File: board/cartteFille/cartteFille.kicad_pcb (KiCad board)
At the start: 2 copper layers, 65 parts, among them U11 MAX4040EUKT, U20 MCP23018-E/SS, U21-2 SN74LVC2G14DBVTG4, U23-4 SN74LVC2G14DBVTG4, U25-6 SN74LVC2G14DBVTG4, U27-8 SN74LVC2G14DBVTG4

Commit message: push sous schémat
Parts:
- moved S27 124.7 mm to (127.5, 147.6)
- moved D25 120.6 mm to (137.9, 96.8)
- moved R253 120.6 mm to (138.0, 96.8)
- moved S25 119.9 mm to (127.8, 94.5)
- moved S28 114.7 mm to (126.7, 120.1)
- moved D26 114.3 mm to (137.7, 68.1)
- moved R263 114.3 mm to (137.7, 68.1)
- moved S26 113.8 mm to (128.0, 65.5)
- moved R261 109.7 mm to (115.6, 68.1)
- moved C261 109.7 mm to (115.6, 73.2)
- moved R251 109.2 mm to (118.1, 82.5)
- moved C251 109.2 mm to (118.1, 87.6)
- moved U25-6 108.8 mm to (107.4, 81.0)
- moved R271 108.2 mm to (119.1, 135.6)
- moved R252 105.9 mm to (128.0, 81.9), turned to 90 degrees
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
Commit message: resistor tab adding
on rajoute une table de résistance pour le changement facile de boutons
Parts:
- moved U21-2 3.75 mm to (44.5, 78.0)

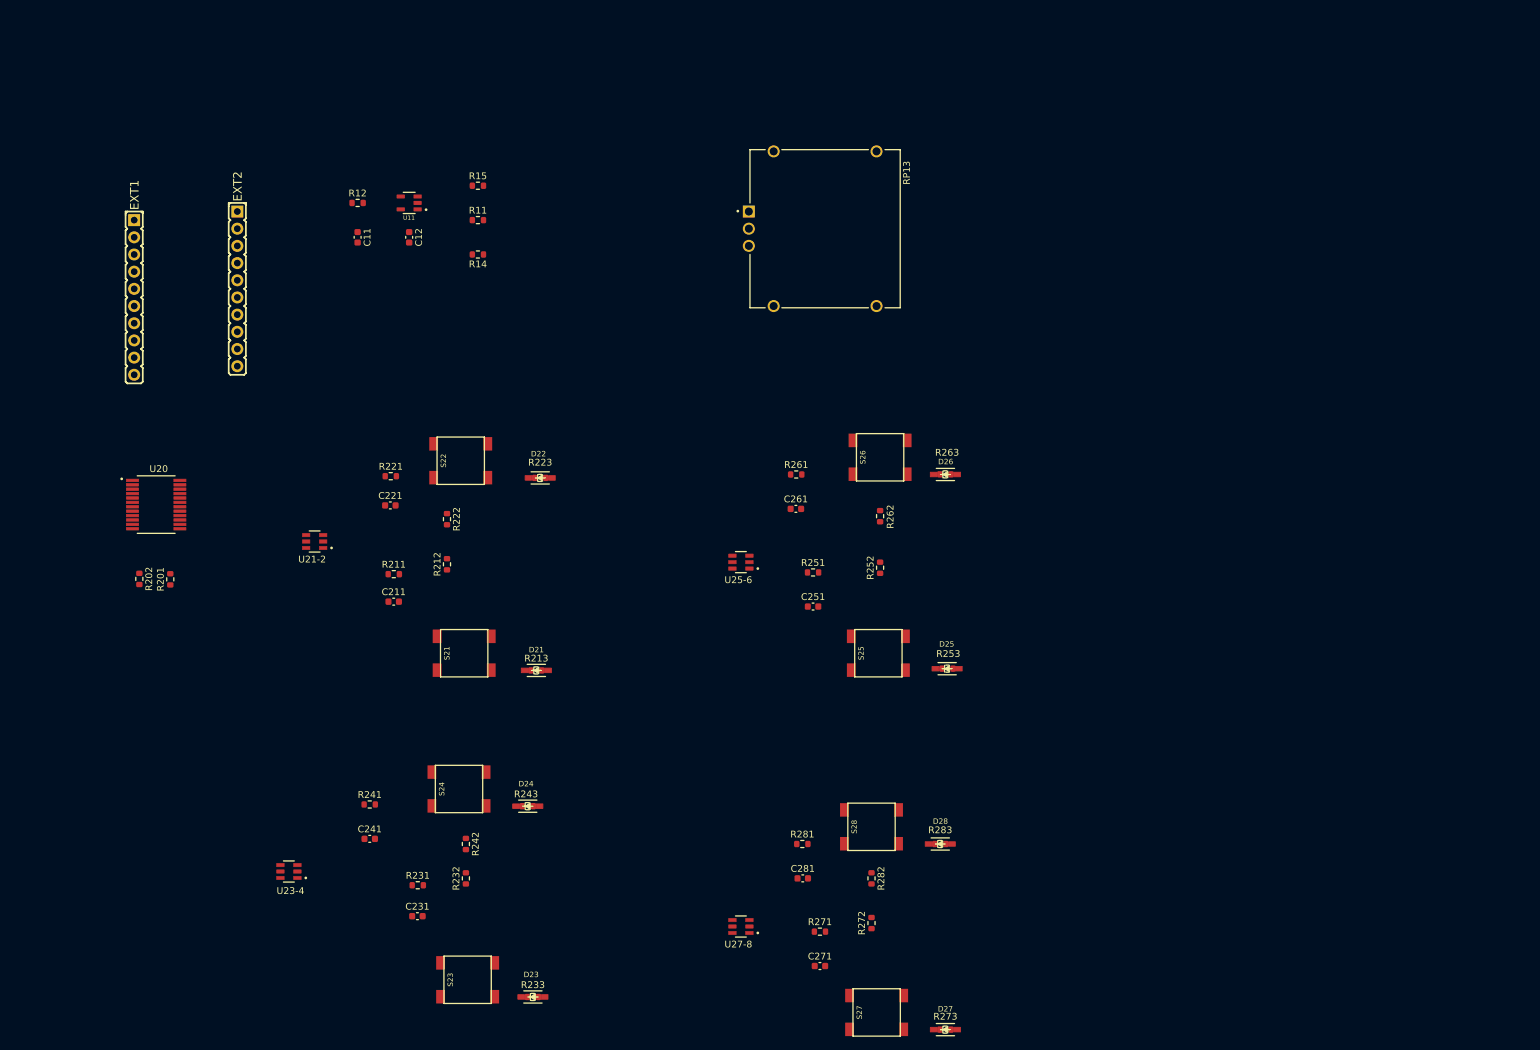
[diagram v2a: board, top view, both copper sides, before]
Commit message: commit début placage
début du placage sans les bouttons
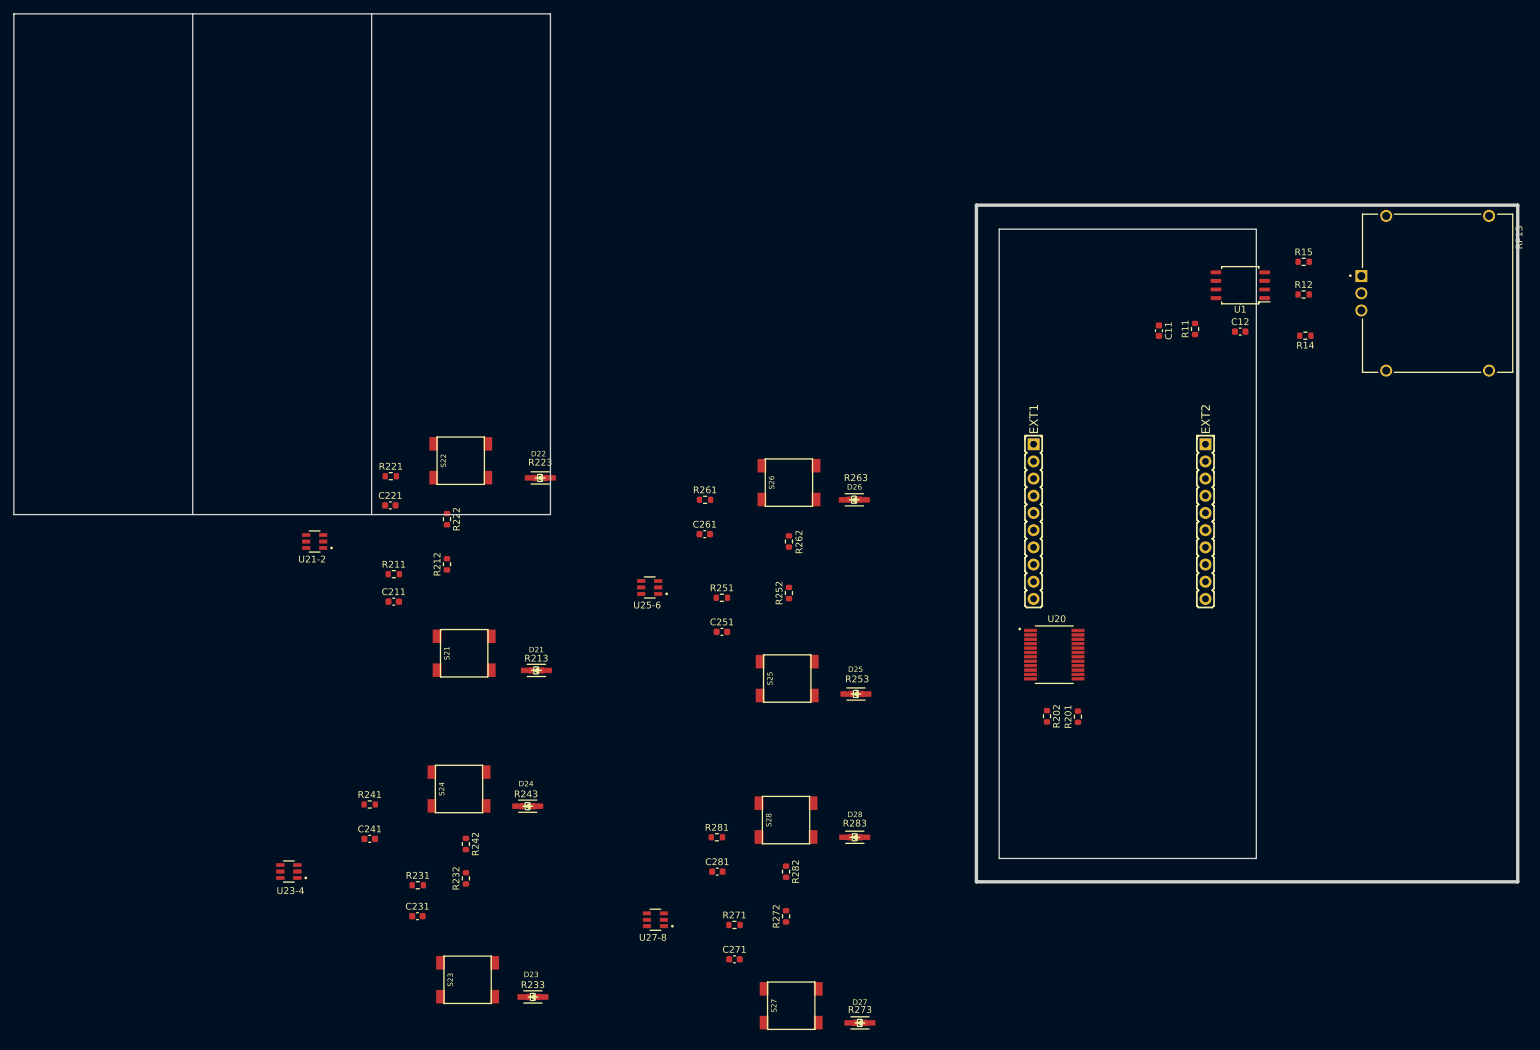
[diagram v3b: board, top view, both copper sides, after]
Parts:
- removed U11: MAX4040EUKT, MAX4040EUKT:SOT95P280X145-5N
- added U1: LM358, Package_SO:SOIC-8_5.275x5.275mm_P1.27mm, F.Cu at (181.2, 40.1)
- R11: value 150Ohm -> 10KOhm
- R12: value 10KOhm -> 150Ohm
- moved EXT2 147.2 mm to (176.1, 75.0)
- moved R12 140.5 mm to (190.6, 41.5)
- moved EXT1 137.0 mm to (150.7, 75.0)
- moved R201 135.7 mm to (157.3, 103.9)
- moved R202 135.7 mm to (152.7, 103.8)
- moved U20 134.6 mm to (153.8, 94.7)
- moved C12 123.6 mm to (181.2, 47.0), turned to 0 degrees
- moved R14 122.9 mm to (190.9, 47.6)
- moved R15 122.5 mm to (190.6, 36.6)
- moved C11 119.2 mm to (169.2, 46.8)
- moved R11 107.2 mm to (174.6, 46.6), turned to 90 degrees
- moved RP13 91.0 mm to (210.4, 41.3)
- moved R253 14.0 mm to (124.5, 100.5)
- moved D26 14.0 mm to (124.2, 71.8)
- moved R261 14.0 mm to (102.1, 71.8)
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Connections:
- EXT1 pad 8: /GPIO3-U20RESET -> unconnected-(EXT1-Pad8)
- EXT2 pad 2: /ADC_CH0-U11RP1 -> unconnected-(EXT2-Pad2)
- EXT2 pad 3: unconnected-(EXT2-Pad3) -> /ADC_CH0-U11RP1
- EXT2 pad 5: /GPIO33-INTA -> unconnected-(EXT2-Pad5)
- R11 pad 1: Net-(R11-Pad1) -> GND
- R11 pad 2: Net-(R11-Pad2) -> /ADC_CH0-U11RP1
- R12 pad 1: /ADC_CH0-U11RP1 -> Net-(R12-Pad1)
- RP13 pad 2: Net-(R11-Pad2) -> Net-(R12-Pad1)
- U20 pad 16: /GPIO33-INTA -> unconnected-(U20-Pad16)
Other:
- board outline added: 222.2 x 128.3 mm

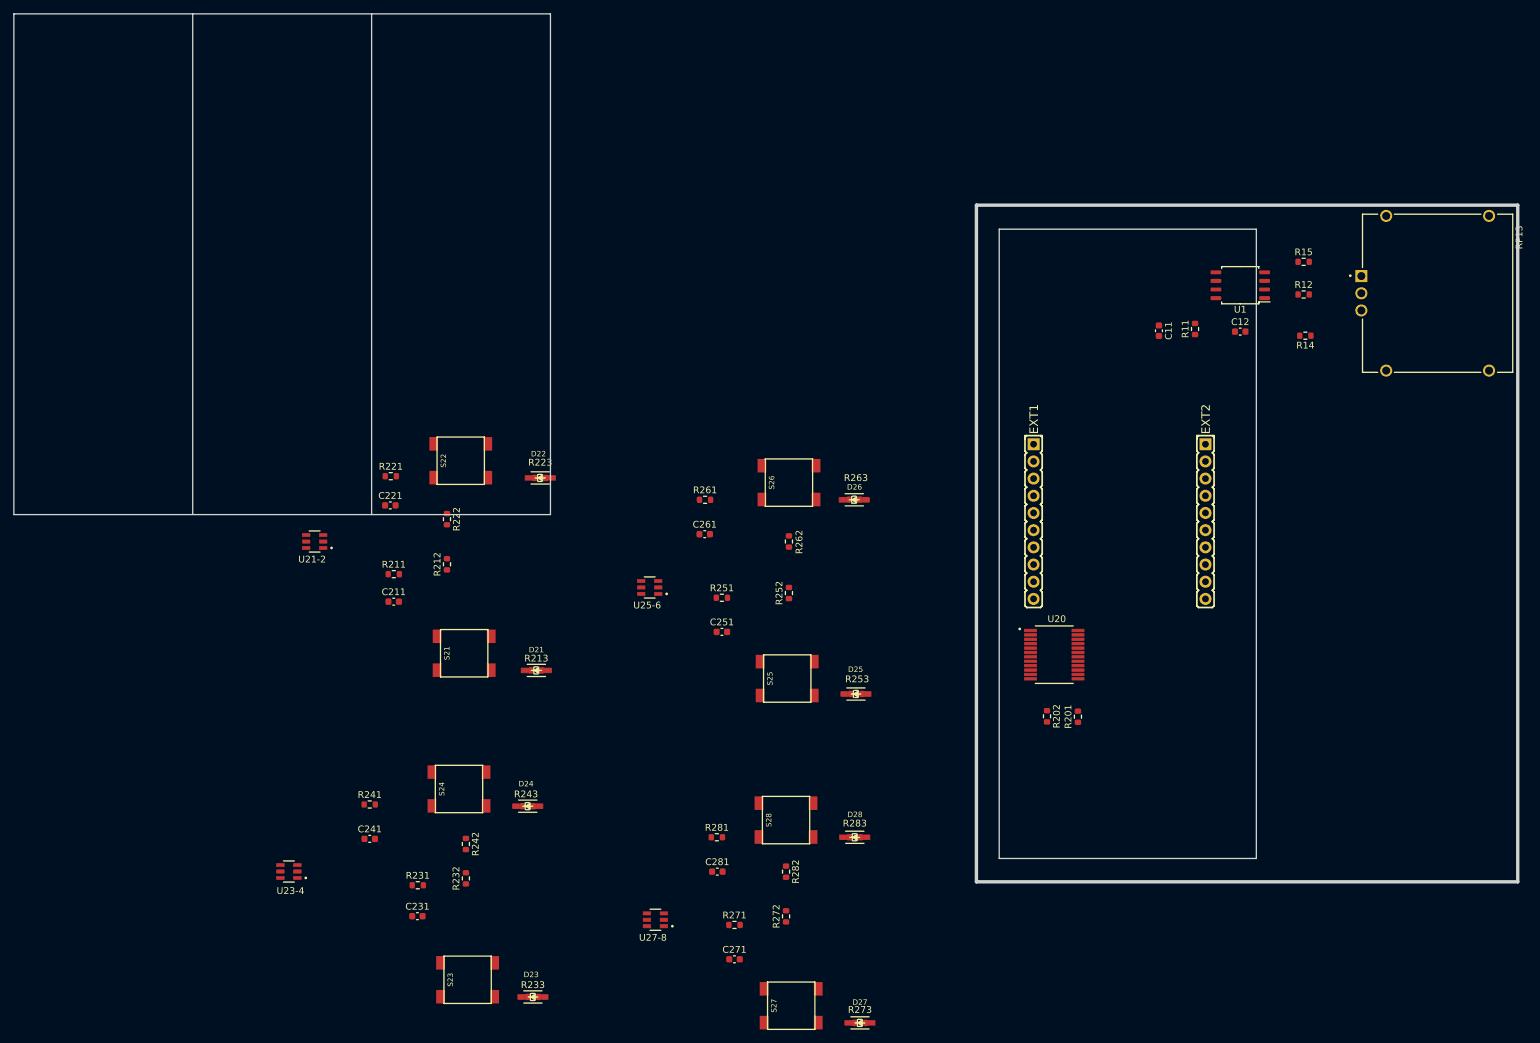
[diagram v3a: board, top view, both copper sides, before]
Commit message: placage de bouton approximatif
tous les composant ont été placé approximativement à des places qui simplifie les connexion entre ceux-ci. Il faudra encore adapter le disign en fonction des dimensions exactes du pcb et des volonté de placement de l'entreprise. puis créer une version clean. pour le moment pcb de 80x100 et placage des bouton en 2 colonnes de 4 botons avec une parie réservée au potentiomètre
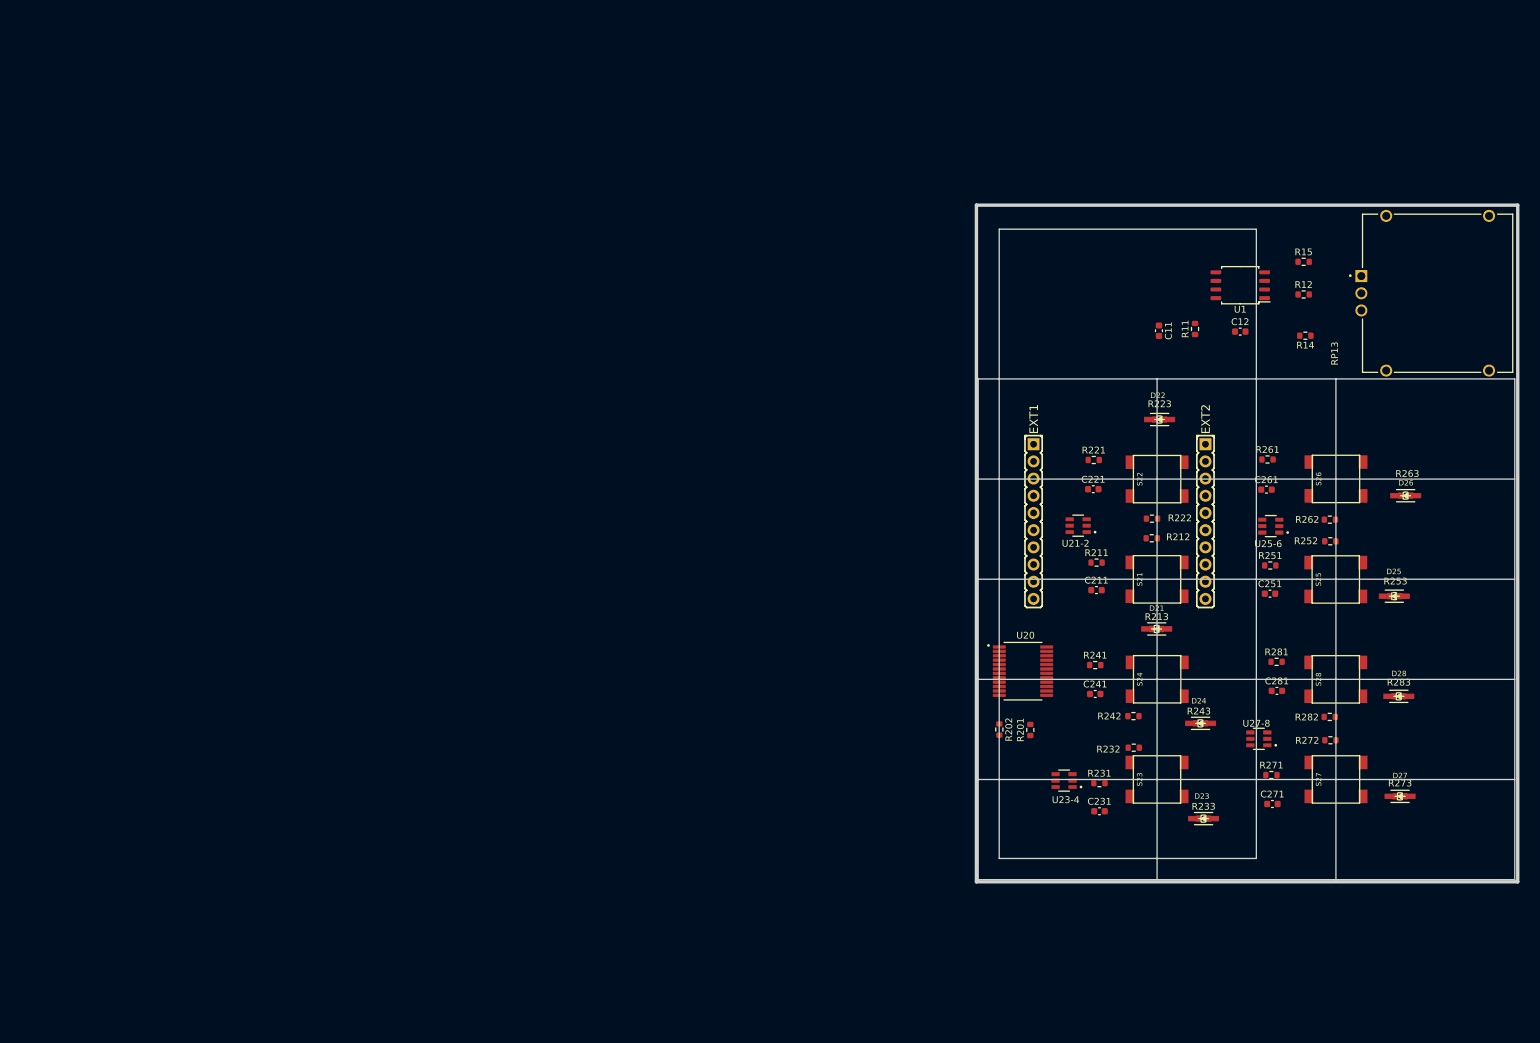
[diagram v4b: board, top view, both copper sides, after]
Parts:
- moved U23-4 115.4 mm to (155.2, 113.3)
- moved U21-2 112.9 mm to (157.3, 75.6)
- moved C241 109.3 mm to (159.8, 100.5)
- moved R241 109.2 mm to (159.8, 96.2)
- moved S23 106.1 mm to (168.9, 113.1)
- moved S24 104.4 mm to (169.0, 98.3)
- moved R212 104.2 mm to (168.2, 77.5), turned to 0 degrees
- moved R222 104.2 mm to (168.2, 74.6), turned to 0 degrees
- moved C221 103.9 mm to (159.5, 70.2)
- moved R221 103.9 mm to (159.6, 65.9)
- moved R211 103.9 mm to (160.0, 81.1)
- moved C211 103.9 mm to (160.0, 85.2)
- moved S21 103.0 mm to (168.9, 83.6)
- moved S22 102.9 mm to (168.9, 68.8)
- moved D23 102.6 mm to (175.8, 118.9)
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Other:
- board size 222.2 x 128.3 mm -> 80 x 100 mm
